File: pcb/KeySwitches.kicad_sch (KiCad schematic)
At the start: 40 parts, among them K1 SW_Push, K10 SW_Push, K11 SW_Push, K12 SW_Push, K13 SW_Push, K14 SW_Push, K15 SW_Push, K16 SW_Push, K17 SW_Push, K18 SW_Push, K2 SW_Push, K3 SW_Push, K4 SW_Push, K5 SW_Push, K6 SW_Push, K7 SW_Push, K8 SW_Push, K9 SW_Push

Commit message: Updated all footprints and libraries to match planned components.
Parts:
- D3: footprint keyboard_parts:D_SOD123_axial -> keebio:Diode-dual
- K1, K10, K11, K12, K13, K14, K15, K16, K17, K18, K2, K3, K4, K5, K6, K7, K8, K9: footprint project_footprints:Kailh_socket_MX_optional_reversible -> keyswitches:Kailh_socket_MX_optional_reversible
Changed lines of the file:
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@@
 			)
 		)
-		(property "Footprint" "project_footprints:Kailh_socket_MX_optional_reversible"
+		(property "Footprint" "keyswitches:Kailh_socket_MX_optional_reversible"
 			(at 50.8 43.18 0)
 			(effects
@@
 			)
 		)
-		(property "Footprint" "project_footprints:Kailh_socket_MX_optional_reversible"
+		(property "Footprint" "keyswitches:Kailh_socket_MX_optional_reversible"
 			(at 91.44 43.18 0)
 			(effects
@@
 			)
 		)
-		(property "Footprint" "project_footprints:Kailh_socket_MX_optional_reversible"
+		(property "Footprint" "keyswitches:Kailh_socket_MX_optional_reversible"
 			(at 129.54 43.18 0)
 			(effects
@@
 			)
 		)
-		(property "Footprint" "project_footprints:Kailh_socket_MX_optional_reversible"
+		(property "Footprint" "keyswitches:Kailh_socket_MX_optional_reversible"
 			(at 167.64 93.98 0)
 			(effects
@@
 			)
 		)
-		(property "Footprint" "project_footprints:Kailh_socket_MX_optional_reversible"
+		(property "Footprint" "keyswitches:Kailh_socket_MX_optional_reversible"
 			(at 91.44 68.58 0)
 			(effects
@@
 			)
 		)
-		(property "Footprint" "project_footprints:Kailh_socket_MX_optional_reversible"
+		(property "Footprint" "keyswitches:Kailh_socket_MX_optional_reversible"
 			(at 205.74 68.58 0)
 			(effects
@@
 			)
 		)
-		(property "Footprint" "project_footprints:Kailh_socket_MX_optional_reversible"
+		(property "Footprint" "keyswitches:Kailh_socket_MX_optional_reversible"
 			(at 205.74 93.98 0)
 			(effects
@@
 			)
 		)
-		(property "Footprint" "project_footprints:Kailh_socket_MX_optional_reversible"
+		(property "Footprint" "keyswitches:Kailh_socket_MX_optional_reversible"
 			(at 167.64 43.18 0)
 			(effects
@@
 			)
 		)
-		(property "Footprint" "project_footprints:Kailh_socket_MX_optional_reversible"
+		(property "Footprint" "keyswitches:Kailh_socket_MX_optional_reversible"
 			(at 205.74 43.18 0)
 			(effects
@@
 			)
 		)
-		(property "Footprint" "keyboard_parts:D_SOD123_axial"
+		(property "Footprint" "keebio:Diode-dual"
 			(at 60.96 48.26 0)
 			(effects
@@
 			)
 		)
-		(property "Footprint" "project_footprints:Kailh_socket_MX_optional_reversible"
+		(property "Footprint" "keyswitches:Kailh_socket_MX_optional_reversible"
 			(at 50.8 93.98 0)
 			(effects
@@
 			)
 		)
-		(property "Footprint" "project_footprints:Kailh_socket_MX_optional_reversible"
+		(property "Footprint" "keyswitches:Kailh_socket_MX_optional_reversible"
 			(at 167.64 68.58 0)
 			(effects
@@
 			)
 		)
-		(property "Footprint" "project_footprints:Kailh_socket_MX_optional_reversible"
+		(property "Footprint" "keyswitches:Kailh_socket_MX_optional_reversible"
 			(at 50.8 68.58 0)
 			(effects
@@
 			)
 		)
-		(property "Footprint" "project_footprints:Kailh_socket_MX_optional_reversible"
+		(property "Footprint" "keyswitches:Kailh_socket_MX_optional_reversible"
 			(at 243.84 68.58 0)
 			(effects
@@
 			)
 		)
-		(property "Footprint" "project_footprints:Kailh_socket_MX_optional_reversible"
+		(property "Footprint" "keyswitches:Kailh_socket_MX_optional_reversible"
 			(at 243.84 93.98 0)
 			(effects
@@
 			)
 		)
-		(property "Footprint" "project_footprints:Kailh_socket_MX_optional_reversible"
+		(property "Footprint" "keyswitches:Kailh_socket_MX_optional_reversible"
 			(at 129.54 68.58 0)
 			(effects
@@
 			)
 		)
-		(property "Footprint" "project_footprints:Kailh_socket_MX_optional_reversible"
+		(property "Footprint" "keyswitches:Kailh_socket_MX_optional_reversible"
 			(at 129.54 93.98 0)
 			(effects
@@
 			)
 		)
-		(property "Footprint" "project_footprints:Kailh_socket_MX_optional_reversible"
+		(property "Footprint" "keyswitches:Kailh_socket_MX_optional_reversible"
 			(at 91.44 93.98 0)
 			(effects
@@
 			)
 		)
-		(property "Footprint" "project_footprints:Kailh_socket_MX_optional_reversible"
+		(property "Footprint" "keyswitches:Kailh_socket_MX_optional_reversible"
 			(at 243.84 43.18 0)
 			(effects

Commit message: Removed Rotary Encoder for space/flippability reasons and replaced all the key switch footprints that weren't bound properly to the schematic for some reason.
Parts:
- removed D1, D2, D6: DIODE, keebio:Diode-dual, symbol pspice:DIODE
- removed ENC1: RotaryEncoder_Switch, Rotary_Encoder:RotaryEncoder_Alps_EC11E-Switch_Vertical_H20mm, symbol Device:RotaryEncoder_Switch
- renumbered D3 to D1, D13 to D10, D14 to D11, D15 to D12, D16 to D13, D17 to D14, D18 to D15, D19 to D16, D20 to D17, D21 to D18, D4 to D2, D5 to D3, D7 to D4, D8 to D5, D9 to D6, D10 to D7, D11 to D8, D12 to D9

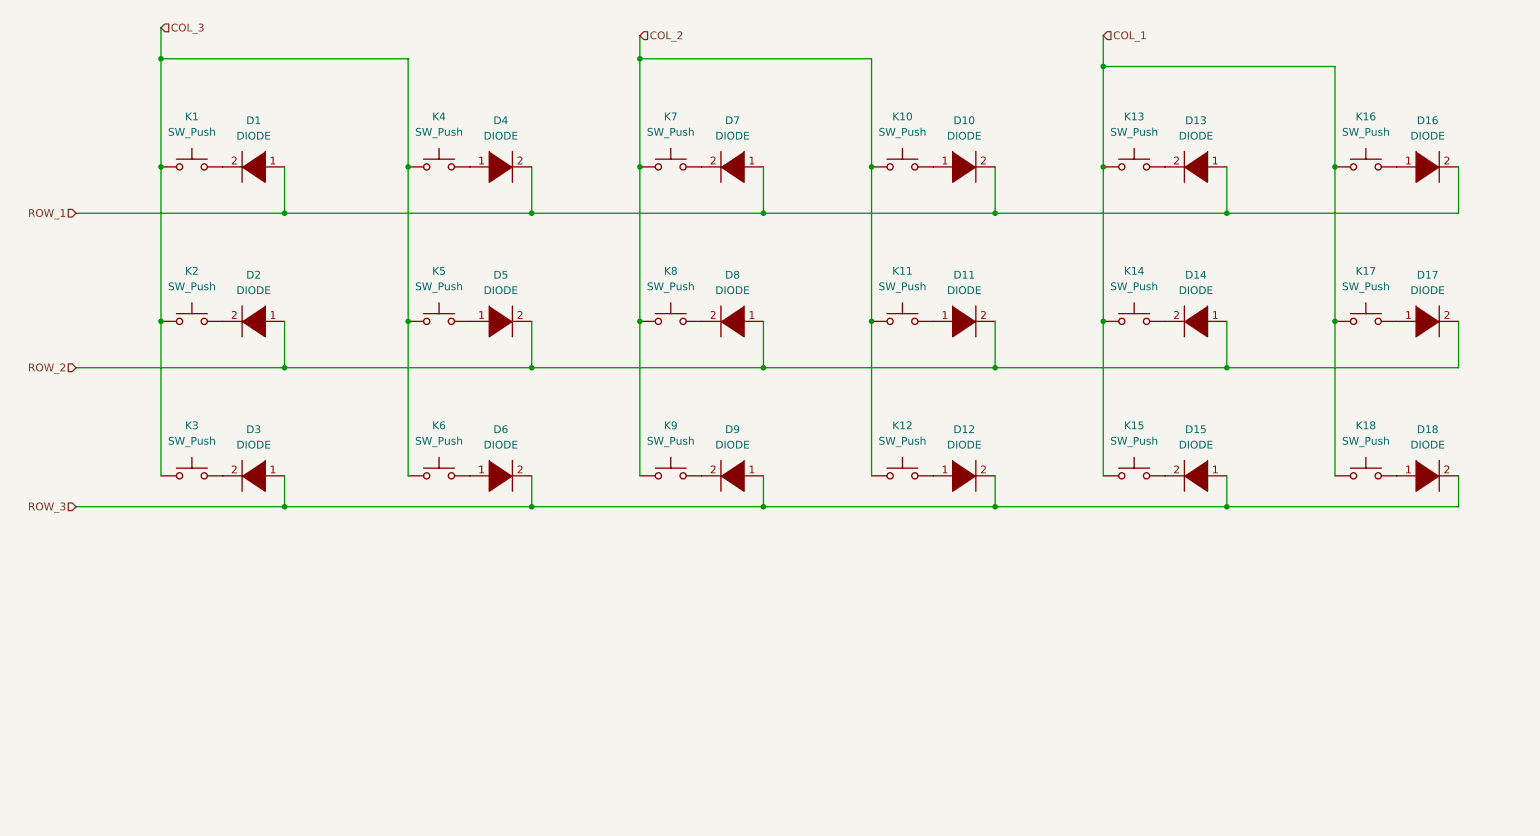
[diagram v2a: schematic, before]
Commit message: Starting to position components and flipping passives as needed. Looking like board size is likely to need to be expanded.
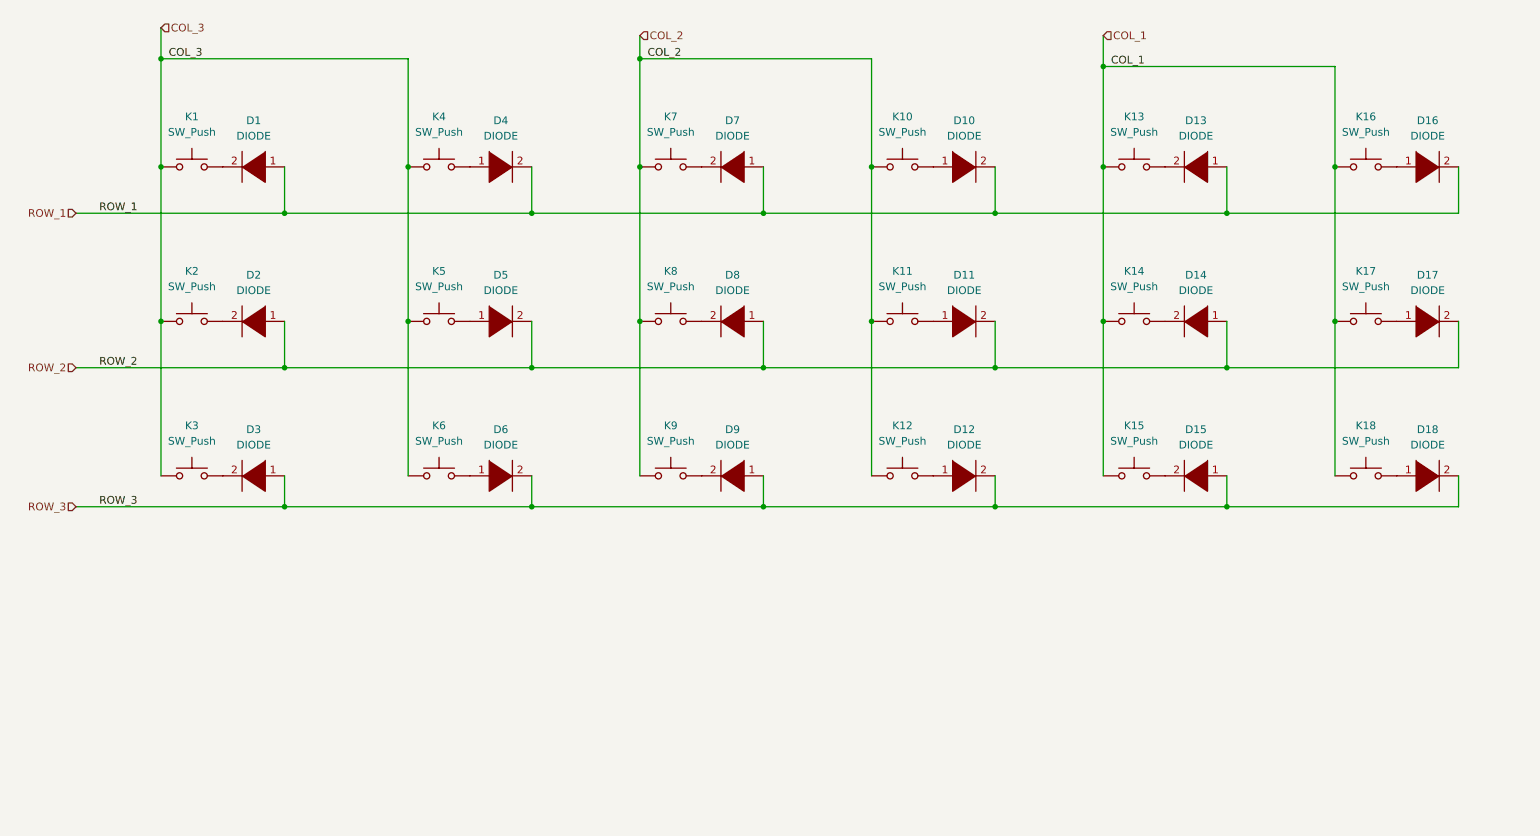
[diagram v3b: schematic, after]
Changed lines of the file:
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@@
+		)
+	)
+	(label "ROW_3"
+		(at 35.56 104.14 0)
+		(fields_autoplaced yes)
+		(effects
+			(font
+				(size 1.27 1.27)
+			)
+			(justify left bottom)
+		)
+	)
+	(label "COL_1"
+		(at 201.93 31.75 0)
+		(fields_autoplaced yes)
+		(effects
+			(font
+				(size 1.27 1.27)
+			)
+			(justify left bottom)
+		)
+	)
+	(label "COL_2"
+		(at 125.73 30.48 0)
+		(fields_autoplaced yes)
+		(effects
+			(font
+				(size 1.27 1.27)
+			)
+			(justify left bottom)
+		)
+	)
+	(label "COL_3"
+		(at 46.99 30.48 0)
+		(fields_autoplaced yes)
+		(effects
+			(font
+				(size 1.27 1.27)
+			)
+			(justify left bottom)
+		)
+	)
+	(label "ROW_2"
+		(at 35.56 81.28 0)
+		(fields_autoplaced yes)
+		(effects
+			(font
+				(size 1.27 1.27)
+			)
+			(justify left bottom)
+		)
+	)
+	(label "ROW_1"
+		(at 35.56 55.88 0)
+		(fields_autoplaced yes)
+		(effects
+			(font
+				(size 1.27 1.27)
+			)
+			(justify left bottom)
 		)
 	)

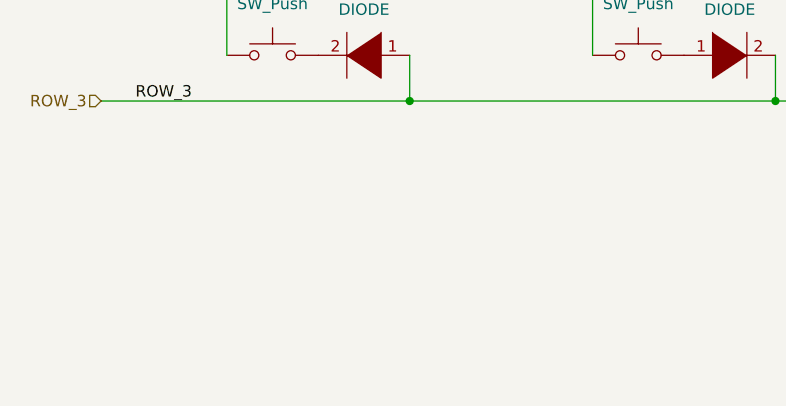
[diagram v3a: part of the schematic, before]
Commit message: WIP: Starting to migrate toward 2 independant halves.
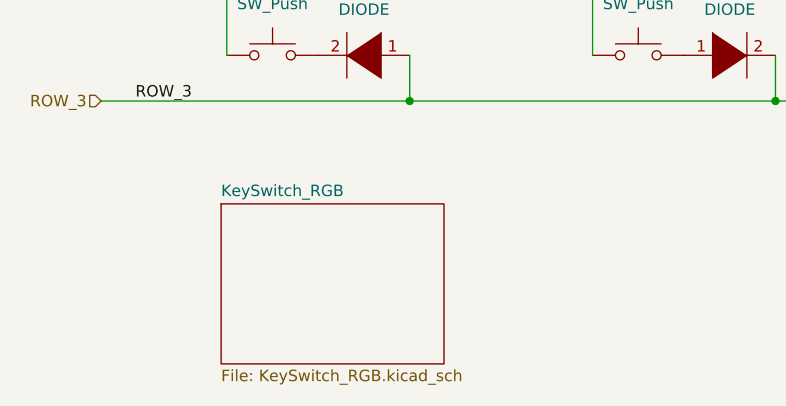
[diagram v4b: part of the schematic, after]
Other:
- added sheet KeySwitch_RGB (KeySwitch_RGB.kicad_sch)
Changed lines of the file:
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@@
+		)
+	)
+	(sheet
+		(at 45.085 115.57)
+		(size 24.765 17.78)
+		(fields_autoplaced yes)
+		(stroke
+			(width 0.1524)
+			(type solid)
+		)
+		(fill
+			(color 0 0 0 0.0000)
+		)
+		(property "Sheetname" "KeySwitch_RGB"
+			(at 45.085 114.8584 0)
+			(effects
+				(font
+					(size 1.27 1.27)
+				)
+				(justify left bottom)
+			)
+		)
+		(property "Sheetfile" "KeySwitch_RGB.kicad_sch"
+			(at 45.085 133.9346 0)
+			(effects
+				(font
+					(size 1.27 1.27)
+				)
+				(justify left top)
+			)
+		)
+		(instances
+			(project "cheapino"
+				(path "/9203b006-47ac-4f34-8cc4-2b709e3df56f/ef93f48f-e975-41f5-b90d-770a980a84dd"
+					(page "7")
+				)
+			)
 		)
 	)

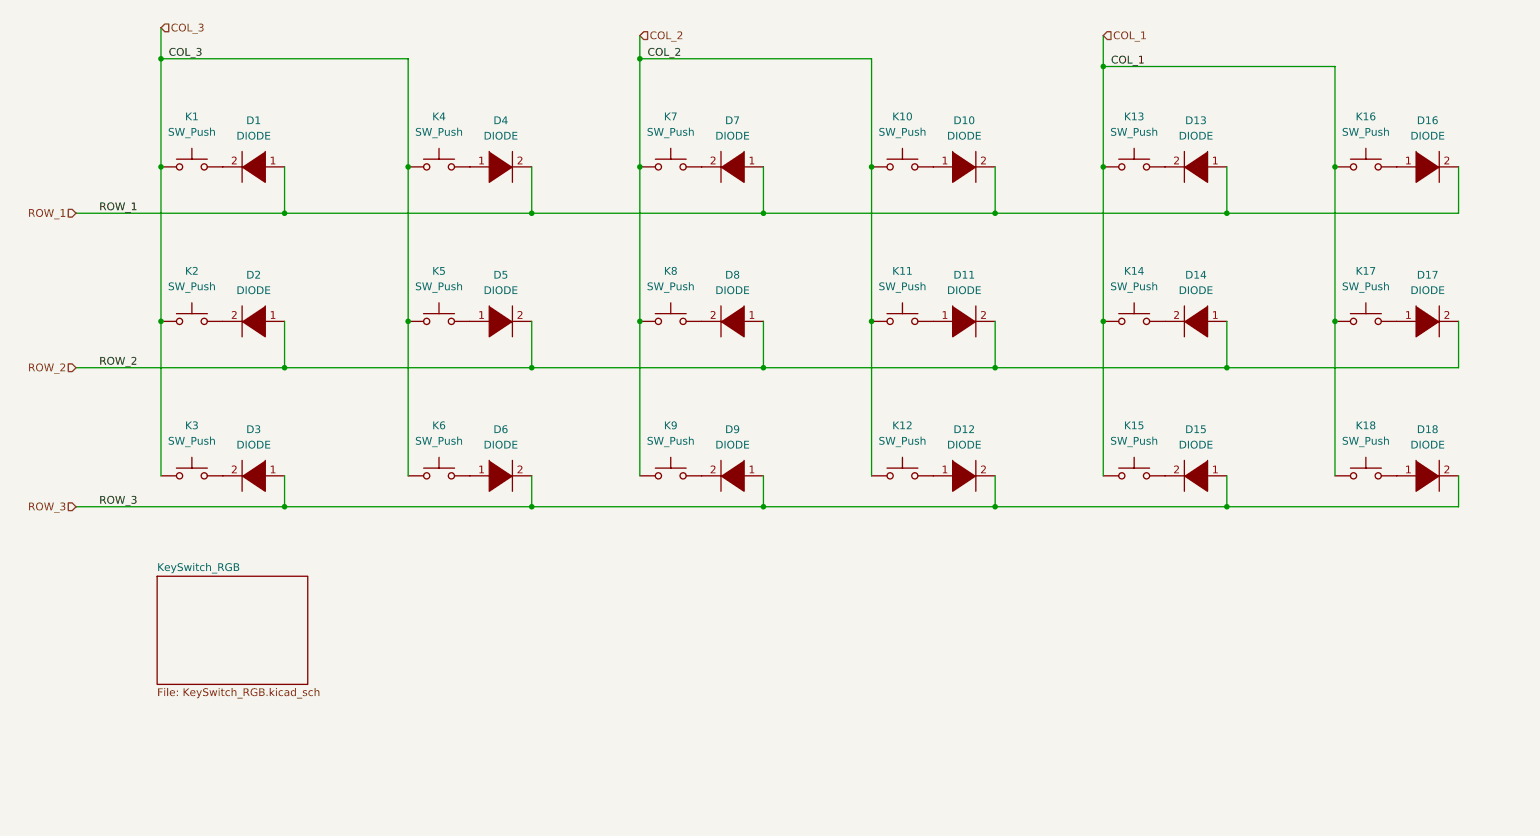
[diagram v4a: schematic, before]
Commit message: WIP: Updating keyboard matrix to use the new shared part and reorganizing all the LED outputs.
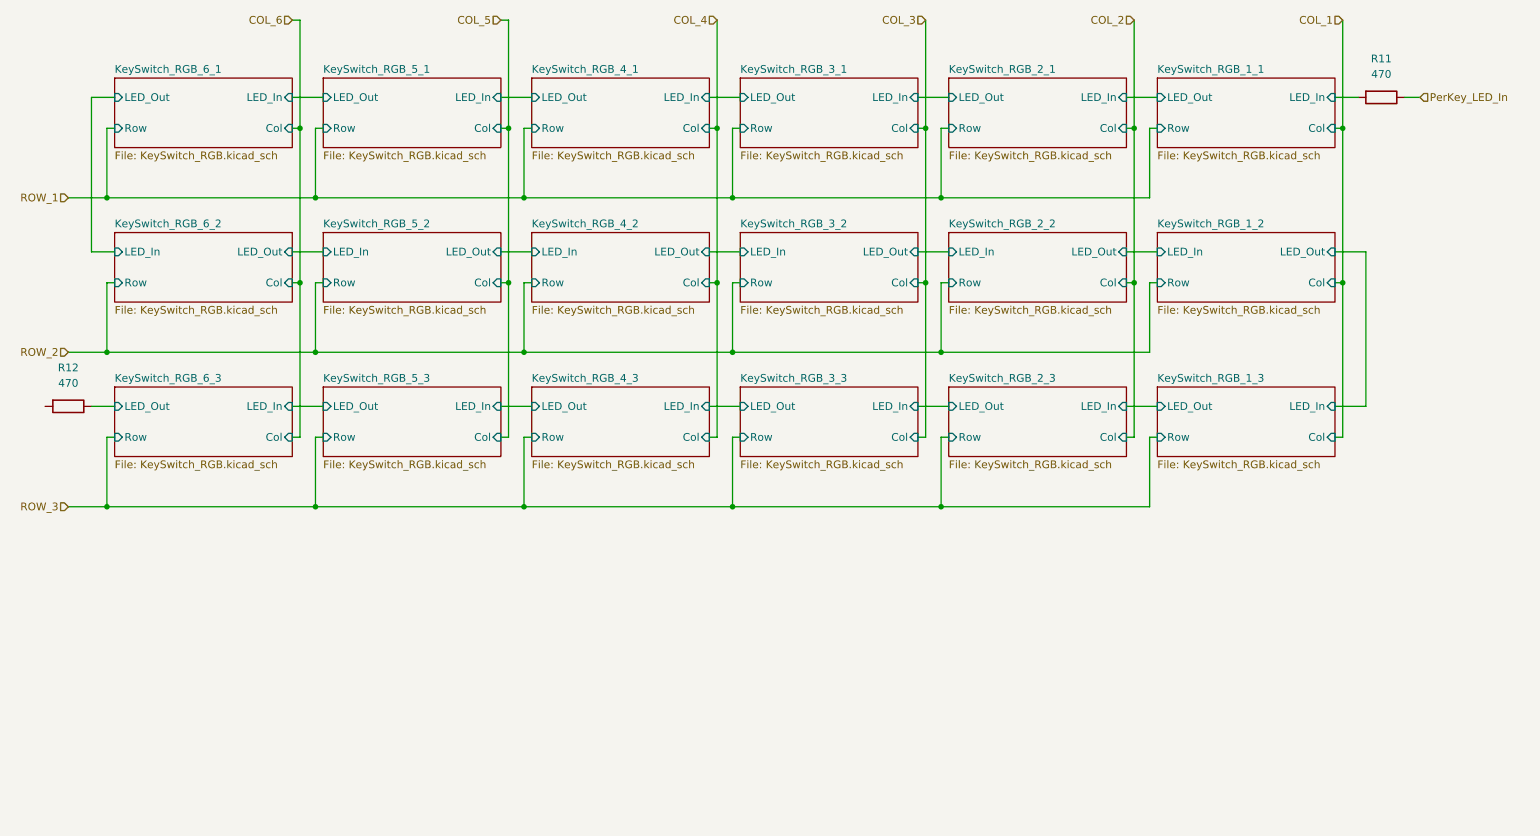
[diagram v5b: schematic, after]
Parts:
- removed D1, D10, D11, D12, D13, D14, D15, D16, D17, D18, D2, D3, D4, D5, D6, D7, D8, D9: DIODE, keebio:Diode-dual, symbol pspice:DIODE
- removed K1, K10, K11, K12, K13, K14, K15, K16, K17, K18, K2, K3, K4, K5, K6, K7, K8, K9: SW_Push, keyswitches:Kailh_socket_MX_optional_reversible, symbol Switch:SW_Push
- added R11, R12: 470, Resistor_SMD:R_0805_2012Metric_Pad1.20x1.40mm_HandSolder, symbol Device:R
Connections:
- new net KeySwitch_RGB_1_1/LED_In: R11.2
- new net KeySwitch_RGB_6_3/LED_Out: R12.1
- new net PerKey_LED_In: R11.1
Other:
- removed sheet KeySwitch_RGB
- added sheet KeySwitch_RGB_1_1 (KeySwitch_RGB.kicad_sch)
- added sheet KeySwitch_RGB_1_2 (KeySwitch_RGB.kicad_sch)
- added sheet KeySwitch_RGB_1_3 (KeySwitch_RGB.kicad_sch)
- added sheet KeySwitch_RGB_2_1 (KeySwitch_RGB.kicad_sch)
- added sheet KeySwitch_RGB_2_2 (KeySwitch_RGB.kicad_sch)
- added sheet KeySwitch_RGB_2_3 (KeySwitch_RGB.kicad_sch)
- added sheet KeySwitch_RGB_3_1 (KeySwitch_RGB.kicad_sch)
- added sheet KeySwitch_RGB_3_2 (KeySwitch_RGB.kicad_sch)
- added sheet KeySwitch_RGB_3_3 (KeySwitch_RGB.kicad_sch)
- added sheet KeySwitch_RGB_4_1 (KeySwitch_RGB.kicad_sch)
- added sheet KeySwitch_RGB_4_2 (KeySwitch_RGB.kicad_sch)
- added sheet KeySwitch_RGB_4_3 (KeySwitch_RGB.kicad_sch)
- added sheet KeySwitch_RGB_5_1 (KeySwitch_RGB.kicad_sch)
- added sheet KeySwitch_RGB_5_2 (KeySwitch_RGB.kicad_sch)
- added sheet KeySwitch_RGB_5_3 (KeySwitch_RGB.kicad_sch)
- added sheet KeySwitch_RGB_6_1 (KeySwitch_RGB.kicad_sch)
- added sheet KeySwitch_RGB_6_2 (KeySwitch_RGB.kicad_sch)
- added sheet KeySwitch_RGB_6_3 (KeySwitch_RGB.kicad_sch)
